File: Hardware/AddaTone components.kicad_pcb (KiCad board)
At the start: 2 copper layers, 60 x 110 mm, 82 parts, among them J1 SWD_Header, J2 Conn_01x20_Female, J3 Conn_01x20_Female, J8 Eurorack_16_pin_power, U1 STM32F446RETx, U2 ICE40UP5K-SG48ITR, U3 MCP6004, U4 PCM5100APW, U5 TL072, U6 LD1117S12TR_SOT223, U7 LM1117-3.3, Y1 ECS-12MHz

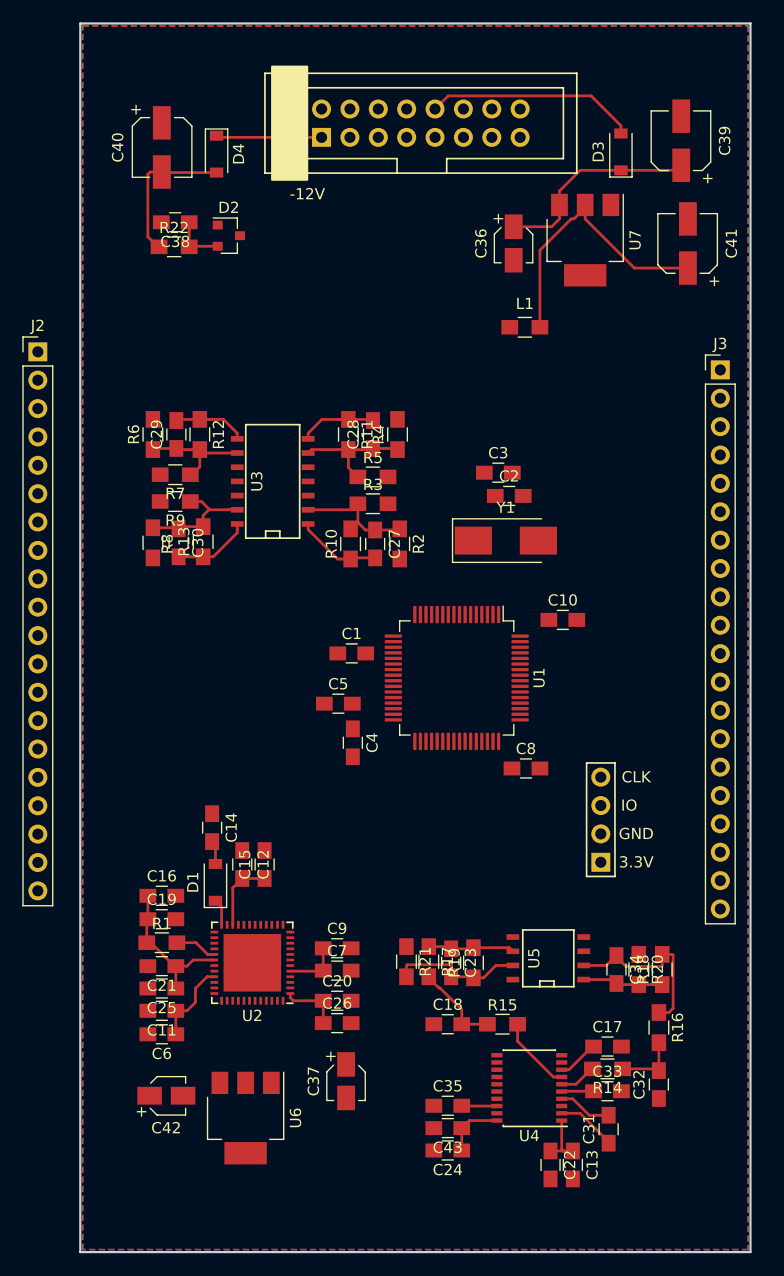
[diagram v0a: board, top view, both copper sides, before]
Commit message: Initial PCB Wiring Completed
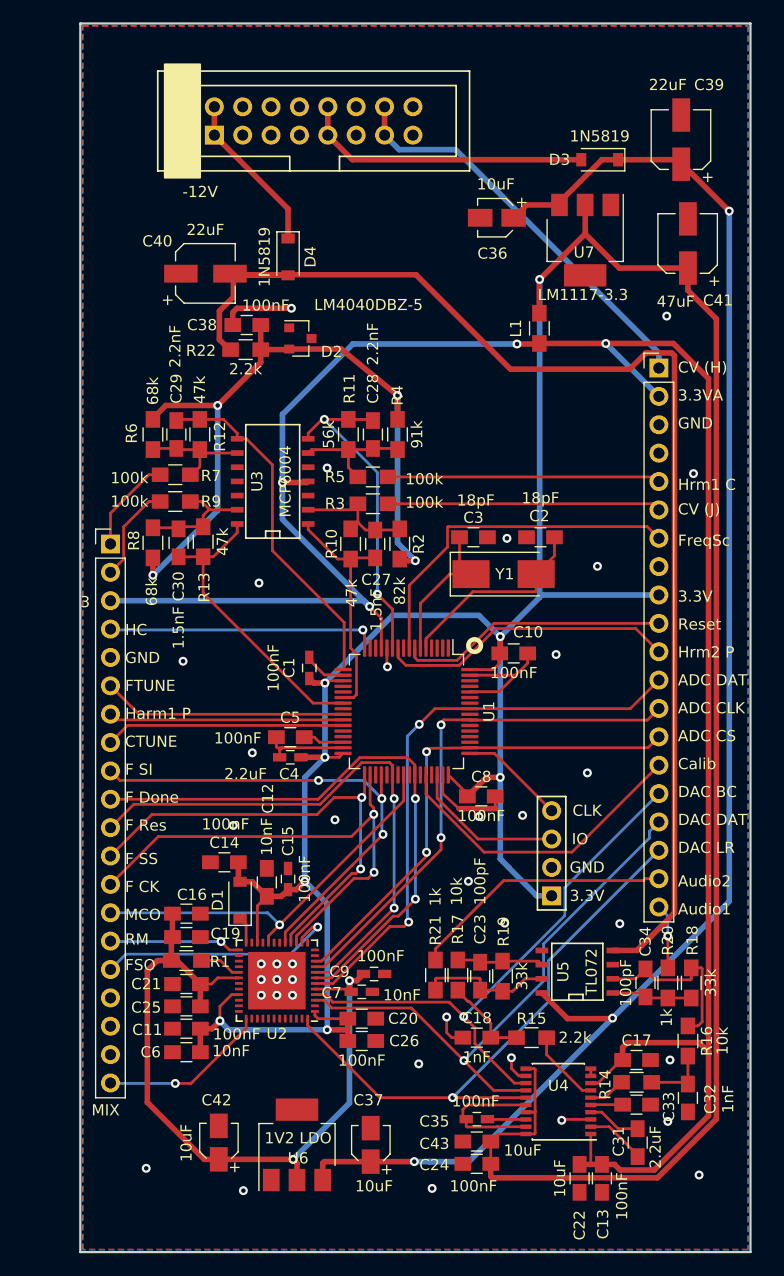
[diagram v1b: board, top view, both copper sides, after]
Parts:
- C1, C15, C35, C4, C7, C9: footprint Capacitors_SMD:C_0805_HandSoldering -> Capacitors_SMD:C_0603_HandSoldering
- U1: value STM32F446RETx -> STM32F446
- U6: value LD1117S12TR_SOT223 -> 1V2 LDO
- moved J2 18.4 mm to (102.7, 96.6)
- moved C40 12.0 mm to (111.2, 72.4), turned to 0 degrees
- moved C38 11.2 mm to (114.9, 77.0)
- moved D2 11.2 mm to (119.7, 78.2)
- moved D4 11.2 mm to (118.6, 70.9)
- moved R22 11.2 mm to (114.8, 79.2)
- moved J8 9.60 mm to (112.0, 60.0)
- moved C42 6.30 mm to (112.4, 150.2), turned to 90 degrees
- moved C3 6.19 mm to (135.2, 96.0)
- moved C37 6.11 mm to (126.0, 150.4), turned to 90 degrees
- moved C4 5.75 mm to (118.8, 115.7), turned to 180 degrees
- moved J3 5.50 mm to (151.8, 80.8)
- moved U1 5.41 mm to (129.2, 111.6)
- moved J1 5.33 mm to (142.2, 128.1)
- moved C10 5.33 mm to (138.8, 106.4)
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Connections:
- J2 pad 1: VCCIO_0 -> HARM2_CVIN
- J2 pad 10: DAC_LRCLK -> FPGA_DONE
- J2 pad 11: ADC_Data -> FPGA_RESET
- J2 pad 12: ADC_Clock -> FPGA_SS
- J2 pad 13: ADC_CS -> FPGA_SCK
- J2 pad 15: RESET -> RING_MOD
- J2 pad 16: FREQ_SCALE_CVIN -> FPGA_SO
- J2 pad 17: HARM2_CVIN -> Net-(J2-Pad17)
- J2 pad 18: GND -> Net-(J2-Pad18)
- J2 pad 19: VCCIO_0 -> Net-(J2-Pad19)
- J2 pad 2: GND -> FREQ_SCALE_CVIN
- J2 pad 20: +3.3VA -> MIX_SWITCH
- J2 pad 3: FPGA_SCK -> +3.3VA
- J2 pad 4: FPGA_SS -> HARM_COUNT
- J2 pad 5: FPGA_SI -> GND
- J2 pad 6: FPGA_DONE -> FTUNE
- J2 pad 7: FPGA_RESET -> HARM1_POT
- J2 pad 8: DAC_DATA -> CTUNE
- J2 pad 9: DAC_BCLK -> FPGA_SI
- J3 pad 1: VCCIO_0 -> CV_IN
- J3 pad 10: FREQ_SC_POT -> RESET
- J3 pad 11: HARM1_POT -> HARM2_POT
- J3 pad 12: HARM2_POT -> ADC_Data
- J3 pad 13: Calibration -> ADC_Clock
- J3 pad 14: RING_MOD -> ADC_CS
- J3 pad 15: MIX_SWITCH -> Calibration
- J3 pad 16: AUDIO1_OUT -> DAC_BCLK
- J3 pad 17: AUDIO2_OUT -> DAC_DATA
- J3 pad 18: VCCIO_0 -> DAC_LRCLK
- J3 pad 19: GND -> AUDIO2_OUT
- J3 pad 2: GND -> +3.3VA
- J3 pad 20: VCCIO_0 -> AUDIO1_OUT
- J3 pad 3: PITCH_CVIN -> GND
- J3 pad 4: HARM1_CVIN -> Net-(J3-Pad4)
- J3 pad 5: CV_IN -> HARM1_CVIN
- J3 pad 6: +1V2 -> PITCH_CVIN
- J3 pad 7: FTUNE -> FREQ_SC_POT
- J3 pad 8: CTUNE -> Net-(J3-Pad8)
- J3 pad 9: HARM_COUNT -> VCCIO_0
- U1 pad 15: HARM1_CV -> Net-(U1-Pad15)
- U1 pad 20: DAC1_OUT -> Net-(U1-Pad20)
- U1 pad 21: DAC2_OUT -> Net-(U1-Pad21)
- U1 pad 22: FREQ_SCALE -> V_OCT_CV
- U1 pad 23: HARM1_POT -> FREQ_SCALE
- U1 pad 24: RING_MOD -> Net-(U1-Pad24)
- U1 pad 26: V_OCT_CV -> HARM1_POT
- U1 pad 38: Net-(U1-Pad38) -> FPGA_RESET
- U1 pad 61: FPGA_RESET -> Net-(U1-Pad61)
- U2 pad 14: Net-(U2-Pad14) -> FPGA_SO
- U2 pad 19: RING_MOD -> Net-(U2-Pad19)
- U2 pad 20: Net-(U2-Pad20) -> MCO2_CLOCK_OUT
- U2 pad 25: Net-(U2-Pad25) -> RING_MOD
- U2 pad 35: MCO2_CLOCK_OUT -> Net-(U2-Pad35)
- U2 pad 37: Net-(U2-Pad37) -> MIX_SWITCH
- U2 pad 45: MIX_SWITCH -> Net-(U2-Pad45)
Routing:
- net VCCIO_0: track 52.1 -> 315.6 mm, vias 0 -> 8
- net +3.3VA: track 9.36 -> 194.7 mm, vias 0 -> 4
- net VCC: track 18.7 -> 141.6 mm, vias 0 -> 3
- net VEE: track 13.2 -> 113.1 mm
- net AREF_-5: track 4.77 -> 67.2 mm, vias 0 -> 4
- net GND: track 0.00 -> 60.6 mm, vias 0 -> 38
- net FPGA_DONE: track 0.00 -> 53.1 mm, vias 0 -> 2
- net DAC_LRCLK: track 0.00 -> 52.6 mm, vias 0 -> 1
- net ADC_Data: track 0.00 -> 52.0 mm, vias 0 -> 2
- net DAC_DATA: track 0.00 -> 50.8 mm, vias 0 -> 1
- net +1V2: track 18.4 -> 68.7 mm, vias 0 -> 2
- net DAC_BCLK: track 0.00 -> 50.2 mm, vias 0 -> 1
- net FPGA_RESET: track 0.00 -> 50.1 mm, vias 0 -> 2
- net ADC_Clock: track 0.00 -> 47.2 mm, vias 0 -> 2
- net FPGA_SCK: track 0.00 -> 45.2 mm, vias 0 -> 2
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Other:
- board text added: "3"
- board text added: "3.3V"
- board text added: "3.3VA"
- board text added: "ADC CLK"
- board text added: "ADC CS"
- board text added: "ADC DAT"
- board text added: "Audio1"
- board text added: "Audio2"
- board text added: "CTUNE"
- board text added: "CV (H)"
- board text added: "CV (J)"
- board text added: "Calib"
- board text added: "DAC BC"
- board text added: "DAC DAT"
- board text added: "DAC LR"
- board text added: "F CK"
- board text added: "F Done"
- board text added: "F Res"
- board text added: "F SI"
- board text added: "F SS"
- board text added: "FSO"
- board text added: "FTUNE"
- board text added: "FreqSc"
- board text added: "GND"
- board text added: "HC"
- board text added: "Harm1 P"
- board text added: "Hrm1 C"
- board text added: "Hrm2 P"
- board text added: "MCO"
- board text added: "MIX"
- board text added: "RM"
- board text added: "Reset"
